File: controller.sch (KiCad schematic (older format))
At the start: 61 parts, among them CON1 SD_Card, IC1 ATMEGA328-A, P1 ISP, P10 RS485, P2 BUTTONS, P3 OPEN_DRAIN, P4 POWER, P5 I2C1, P6 I2C2, P7 CONN_01X05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

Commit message: Use 4050 as a level shifter
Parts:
- removed U3: 74LS125, Housings_SOIC:SOIC-14_3.9x8.7mm_Pitch1.27mm, symbol 74LS125
- added U3: 4050, Housings_SSOP:TSSOP-16_4.4x5mm_Pitch0.65mm, symbol 4050
- C15: footprint (none) -> Capacitors_SMD:C_0603_HandSoldering
- P7: footprint (none) -> Pin_Headers:Pin_Header_Straight_1x05
- R12, R7: footprint (none) -> Resistors_SMD:R_0603_HandSoldering

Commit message: Add protection
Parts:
- added D? (x3): TVS-DUAL, symbol TVS-DUAL
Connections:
- wire segments 147 -> 155
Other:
- moved on the sheet: JP1, R12, R5, R7

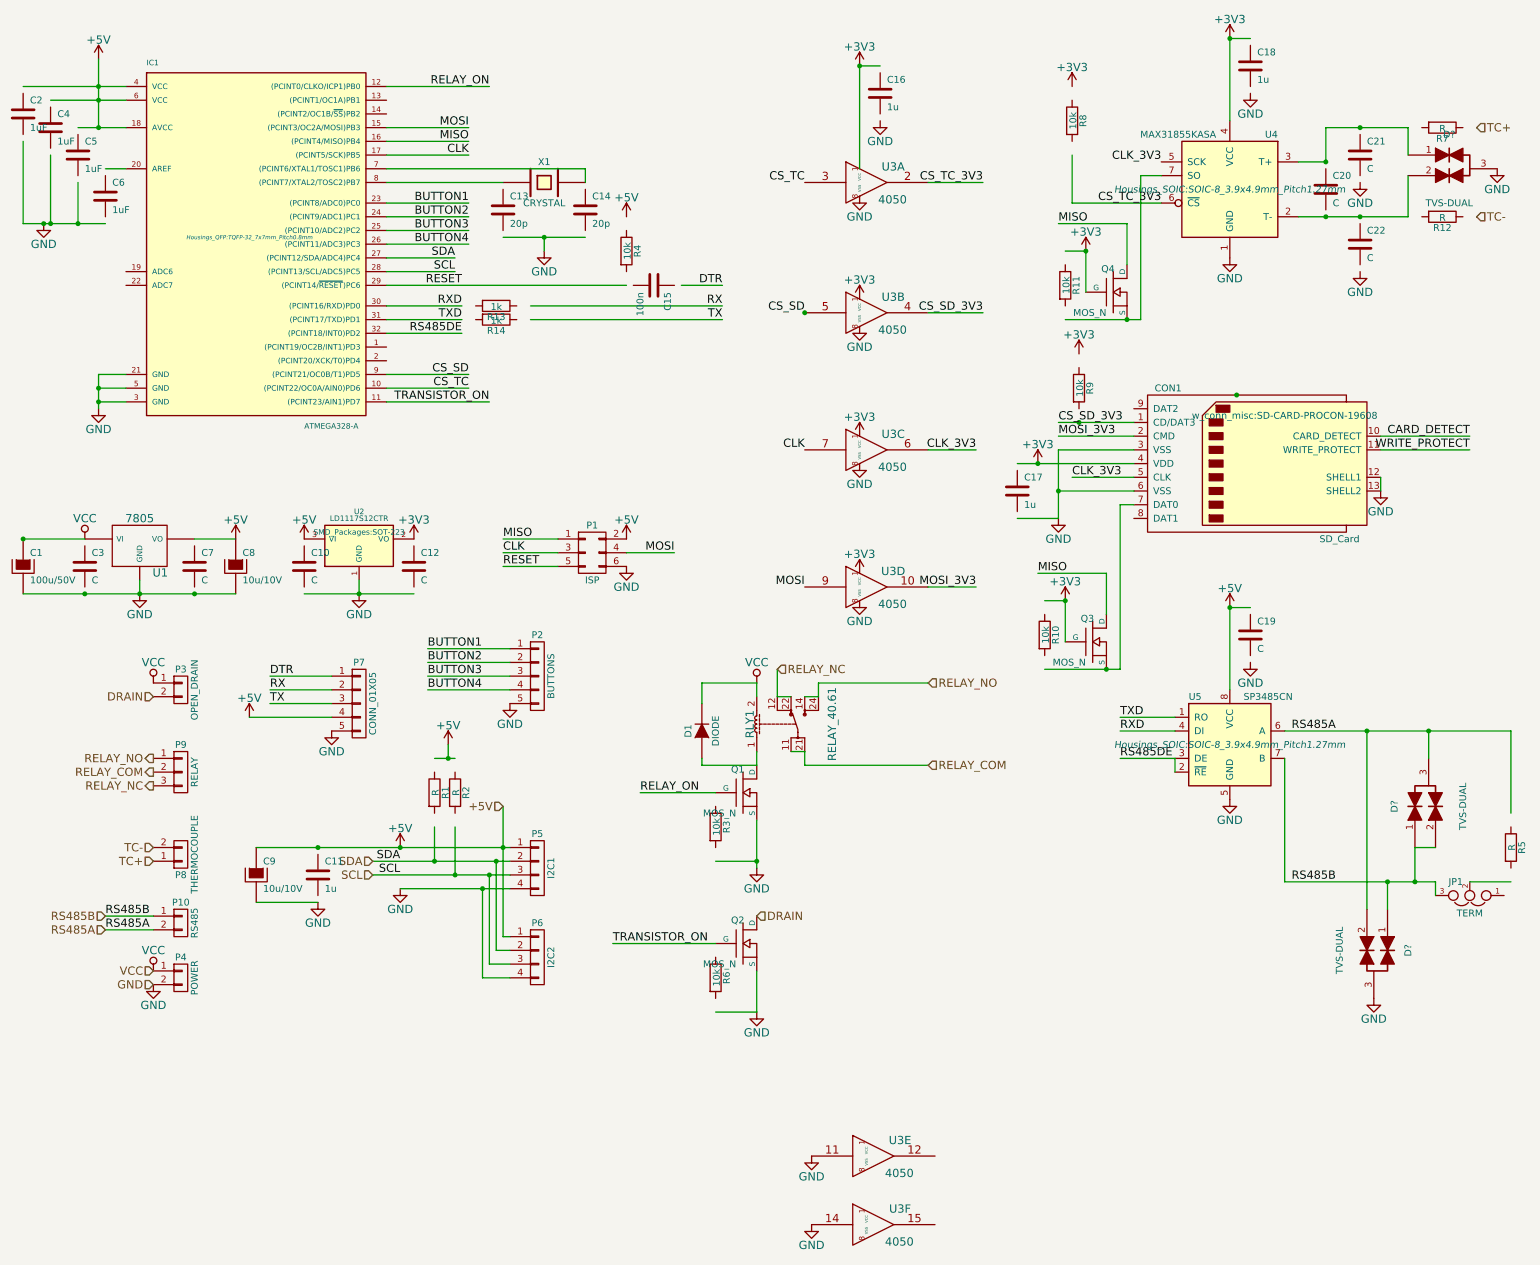
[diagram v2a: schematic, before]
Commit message: Fix schematics after kicad library upgrade
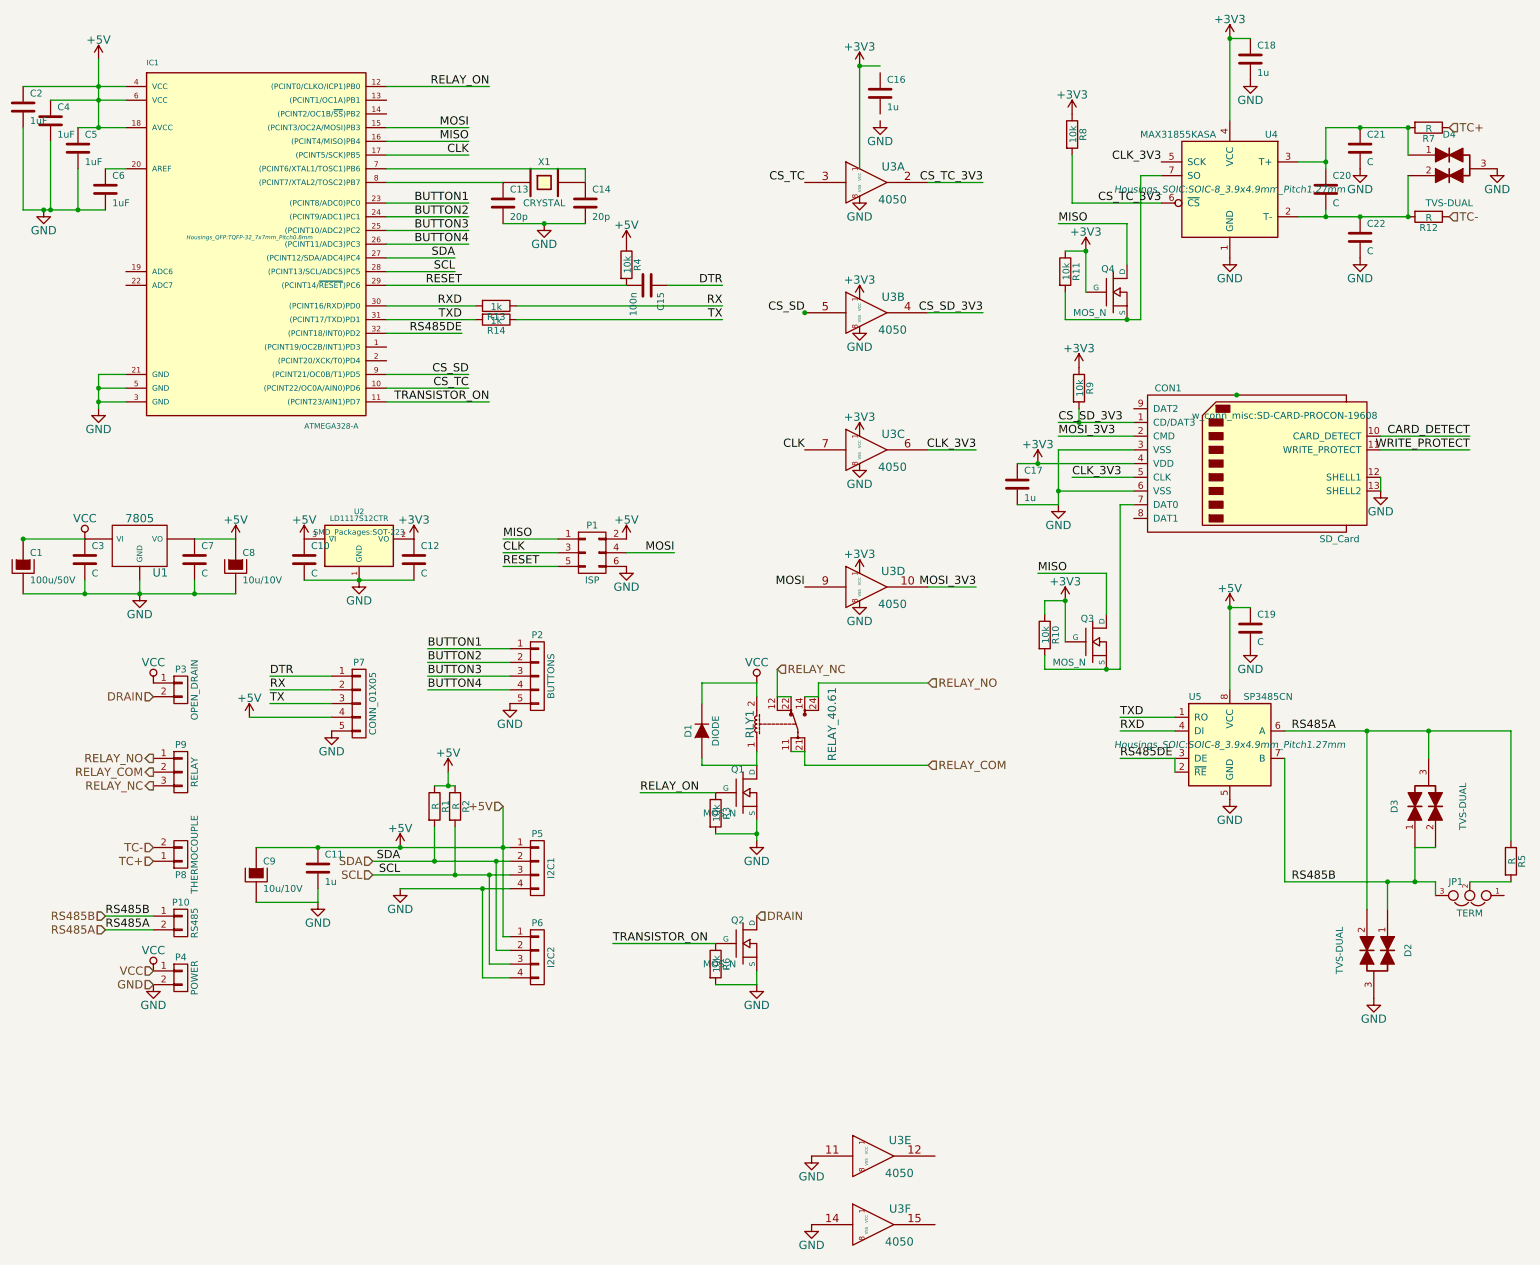
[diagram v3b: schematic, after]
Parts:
- D2, D3, D4: renamed from D?; footprint (none) -> SMD_Packages:SOT-323
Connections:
- wire segments 155 -> 203
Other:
- moved on the sheet: C10, C11, C12, C13, C14, C15, C17, C18, C19, C2, C21, C22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

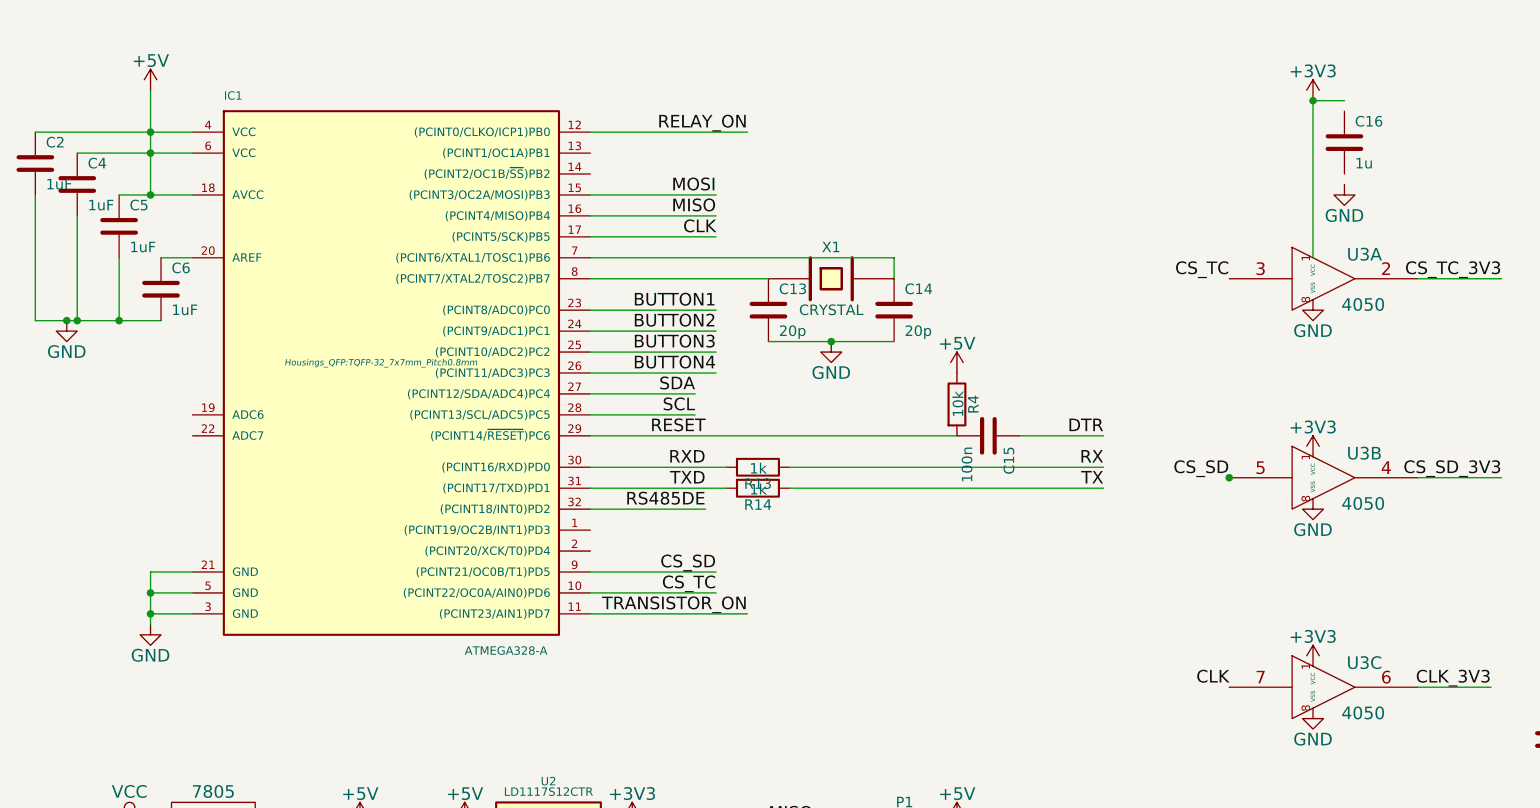
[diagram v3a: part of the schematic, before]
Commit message: Fix missing ground connection. Change the MCU to Atmega328P for better Arduino compatibility
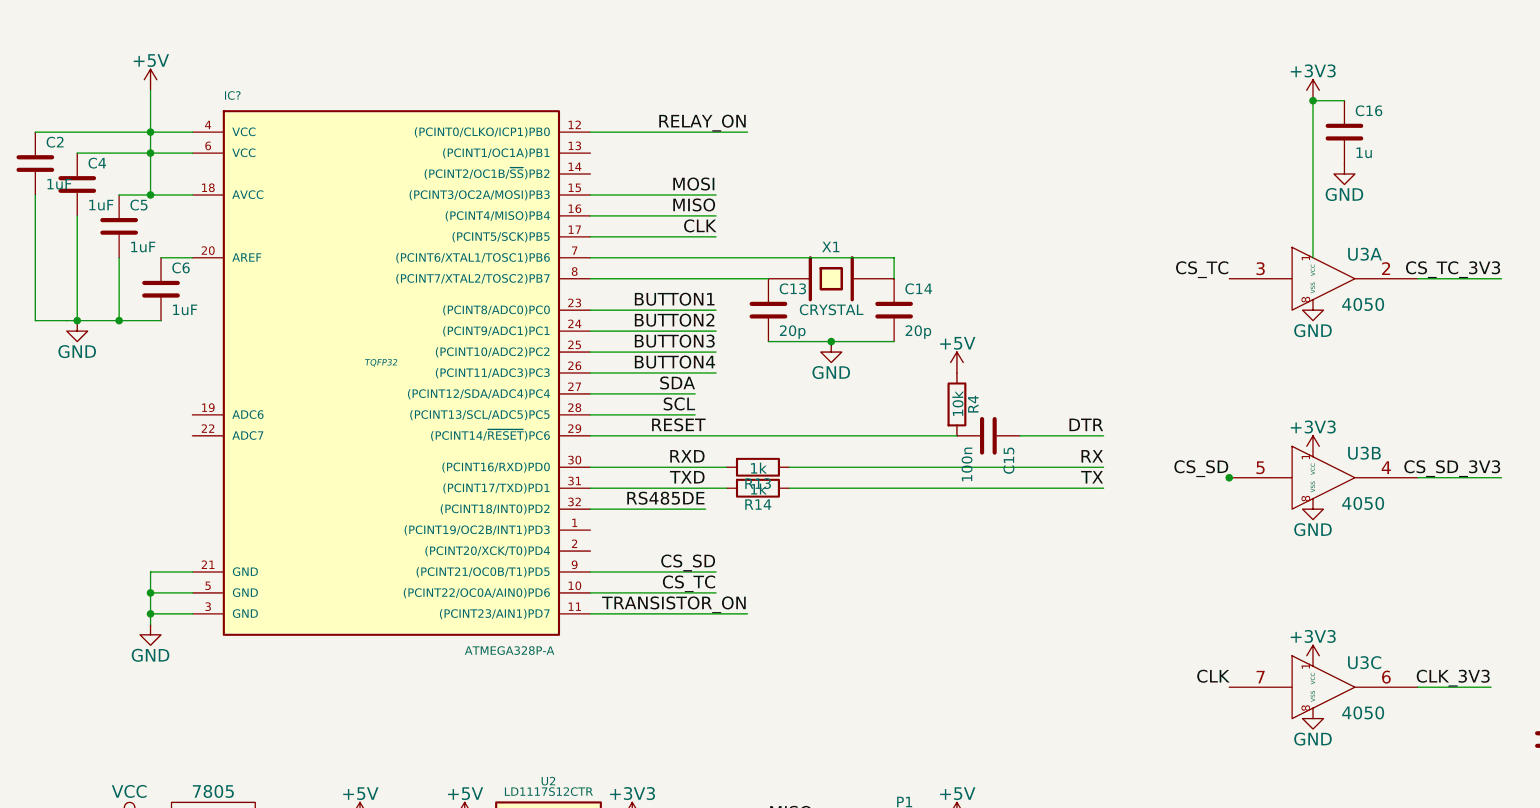
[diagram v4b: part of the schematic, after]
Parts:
- removed IC1: ATMEGA328-A, Housings_QFP:TQFP-32_7x7mm_Pitch0.8mm, symbol ATMEGA328-A
- added IC?: ATMEGA328P-A, TQFP32, symbol ATMEGA328P-A
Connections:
- net +3V3: now also C16.1
- net +5V: now also IC?.18 (AVCC), IC?.4 (VCC), IC?.6 (VCC)
- net BUTTON1: now also IC?.23 ((PCINT8/ADC0)PC0)
- net BUTTON2: now also IC?.24 ((PCINT9/ADC1)PC1)
- net BUTTON3: now also IC?.25 ((PCINT10/ADC2)PC2)
- net BUTTON4: now also IC?.26 ((PCINT11/ADC3)PC3)
- net CLK: now also IC?.17 ((PCINT5/SCK)PB5)
- net CS_SD: now also IC?.9 ((PCINT21/OC0B/T1)PD5)
- net CS_TC: now also IC?.10 ((PCINT22/OC0A/AIN0)PD6)
- net GND: now also C16.2, IC?.21 (GND), IC?.3 (GND), IC?.5 (GND)
- net MISO: now also IC?.16 ((PCINT4/MISO)PB4)
- net MOSI: now also IC?.15 ((PCINT3/OC2A/MOSI)PB3)
- net RELAY_ON: now also IC?.12 ((PCINT0/CLKO/ICP1)PB0)
- net RESET: now also IC?.29 ((PCINT14/~RESET~)PC6)
- net RS485DE: now also IC?.32 ((PCINT18/INT0)PD2)
- net RXD: now also IC?.30 ((PCINT16/RXD)PD0)
- net SCL: now also IC?.28 ((PCINT13/SCL/ADC5)PC5)
- net SDA: now also IC?.27 ((PCINT12/SDA/ADC4)PC4)
- net TRANSISTOR_ON: now also IC?.11 ((PCINT23/AIN1)PD7)
- net TXD: now also IC?.31 ((PCINT17/TXD)PD1)
- net at C6.1: now also IC?.20 (AREF)
- net at C14.1, X1.2: now also IC?.7 ((PCINT6/XTAL1/TOSC1)PB6)
- net at C13.1, X1.1: now also IC?.8 ((PCINT7/XTAL2/TOSC2)PB7)
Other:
- moved on the sheet: C16
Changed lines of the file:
@@
 $EndDescr
-$Comp
-L ATMEGA328-A IC1
-U 1 1 54E5BB29
-P 2300 2100
-F 0 "IC1" H 1550 3350 40  0000 L BNN
-F 1 "ATMEGA328-A" H 2700 700 40  0000 L BNN
-F 2 "Housings_QFP:TQFP-32_7x7mm_Pitch0.8mm" H 2300 2100 30  0000 C CIN
-F 3 "" H 2300 2100 60  0000 C CNN
-	1    2300 2100
-	1    0    0    -1
-$EndComp
 $Comp
 L MAX31855KASA U4
@@
 L GND #PWR02
 U 1 1 54E5BF8F
-P 800 1900
-F 0 "#PWR02" H 800 1650 60  0001 C CNN
-F 1 "GND" H 800 1750 60  0000 C CNN
-F 2 "" H 800 1900 60  0000 C CNN
-F 3 "" H 800 1900 60  0000 C CNN
-	1    800  1900
+P 850 1900
+F 0 "#PWR02" H 850 1650 60  0001 C CNN
+F 1 "GND" H 850 1750 60  0000 C CNN
+F 2 "" H 850 1900 60  0000 C CNN
+F 3 "" H 850 1900 60  0000 C CNN
+	1    850  1900
 	1    0    0    -1
 $EndComp
@@
 L C C16
 U 1 1 54E6857A
-P 6900 1050
-F 0 "C16" H 6950 1150 50  0000 L CNN
-F 1 "1u" H 6950 950 50  0000 L CNN
-F 2 "Capacitors_SMD:C_0603_HandSoldering" H 6938 900 30  0001 C CNN
-F 3 "" H 6900 1050 60  0000 C CNN
-	1    6900 1050
+P 6900 1000
+F 0 "C16" H 6950 1100 50  0000 L CNN
+F 1 "1u" H 6950 900 50  0000 L CNN
+F 2 "Capacitors_SMD:C_0603_HandSoldering" H 6938 850 30  0001 C CNN
+F 3 "" H 6900 1000 60  0000 C CNN
+	1    6900 1000
 	1    0    0    -1
 $EndComp
@@
 L GND #PWR031
 U 1 1 54E68580
-P 6900 1250
-F 0 "#PWR031" H 6900 1000 60  0001 C CNN
-F 1 "GND" H 6900 1100 60  0000 C CNN
-F 2 "" H 6900 1250 60  0000 C CNN
-F 3 "" H 6900 1250 60  0000 C CNN
-	1    6900 1250
+P 6900 1150
+F 0 "#PWR031" H 6900 900 60  0001 C CNN
+F 1 "GND" H 6900 1000 60  0000 C CNN
+F 2 "" H 6900 1150 60  0000 C CNN
+F 3 "" H 6900 1150 60  0000 C CNN
+	1    6900 1150
 	1    0    0    -1
 $EndComp
@@
 Wire Wire Line
 	650  1900 650  1300
-Connection ~ 800  1900
 Wire Wire Line
 	1200 3300 1400 3300
@@
 Wire Wire Line
 	5700 6450 5700 6450
+$Comp
+L ATMEGA328P-A IC?
+U 1 1 5521429B
+P 2300 2100
+F 0 "IC?" H 1550 3350 40  0000 L BNN
+F 1 "ATMEGA328P-A" H 2700 700 40  0000 L BNN
+F 2 "TQFP32" H 2300 2100 30  0000 C CIN
+F 3 "" H 2300 2100 60  0000 C CNN
+	1    2300 2100
+	1    0    0    -1
+$EndComp
 $EndSCHEMATC
